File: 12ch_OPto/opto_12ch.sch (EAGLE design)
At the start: 66 parts, among them J1 RJMG2310228A0ER, J2 RJMG2310228A0ER, U10 PCF8575PWRE4, U19 MOC3063S, U20 MOC3063S, U21 MOC3063S, U22 MOC3063S, U23 MOC3063S, U24 MOC3063S, U25 MOC3063S, U26 MOC3063S, U27 LM317, U29 Z0103MN, U30 Z0103MN, U31 Z0103MN, U32 Z0103MN, U33 Z0103MN, U34 Z0103MN, U35 Z0103MN, U36 Z0103MN, X1 TSW-101-07-G-D

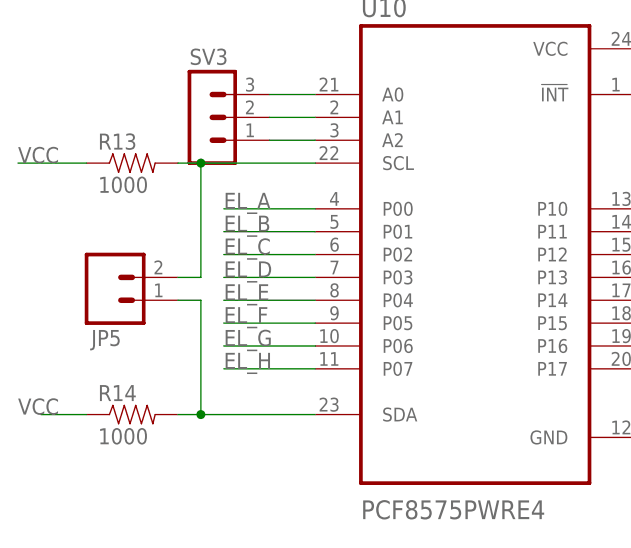
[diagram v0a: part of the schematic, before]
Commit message: optimiz
Se redujo lo mayor posible las dimensiones de la placa
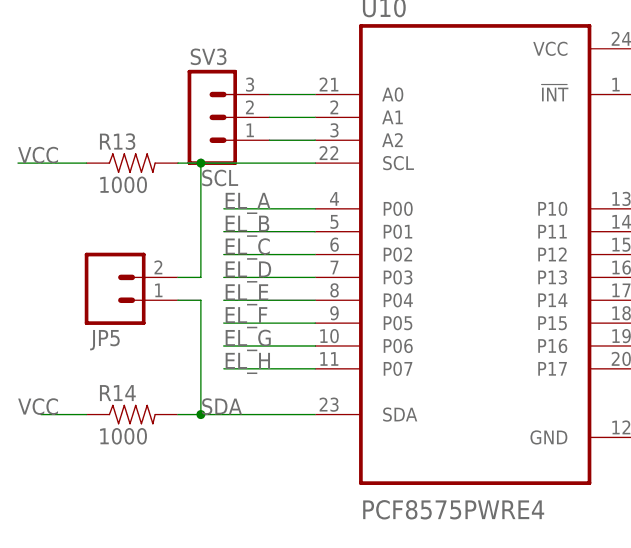
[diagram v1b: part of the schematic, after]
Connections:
- net N$21 renamed SCL
- net N$22 renamed SDA
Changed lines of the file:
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@@
 </segment>
 </net>
-<net name="N$21" class="0">
+<net name="SCL" class="0">
 <segment>
 <pinref part="U10" gate="A" pin="SCL"/>
@@
 <wire x1="-203.2" y1="7.62" x2="-203.2" y2="20.32" width="0.1524" layer="91"/>
 <junction x="-203.2" y="20.32"/>
+<label x="-203.2" y="17.78" size="1.778" layer="95"/>
 </segment>
 </net>
-<net name="N$22" class="0">
+<net name="SDA" class="0">
 <segment>
 <pinref part="U10" gate="A" pin="SDA"/>
@@
 <wire x1="-203.2" y1="5.08" x2="-203.2" y2="-7.62" width="0.1524" layer="91"/>
 <junction x="-203.2" y="-7.62"/>
+<label x="-203.2" y="-7.62" size="1.778" layer="95"/>
 </segment>
 </net>
